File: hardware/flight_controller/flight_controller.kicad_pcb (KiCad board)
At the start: 2 copper layers, 2 parts, among them U1 Teensy3.6

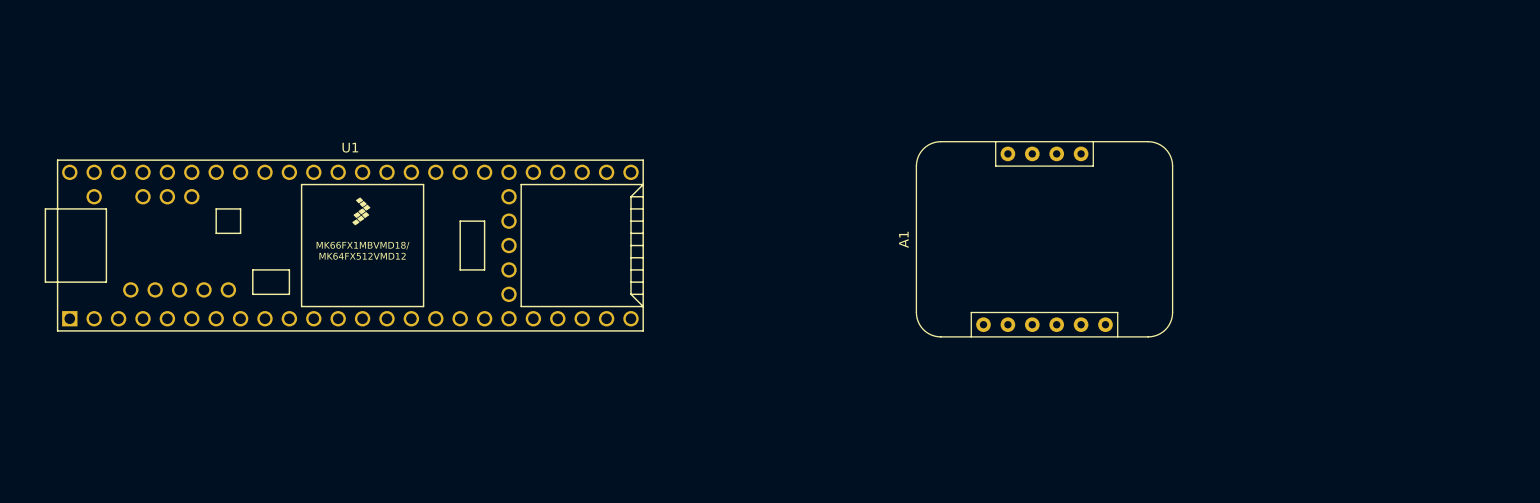
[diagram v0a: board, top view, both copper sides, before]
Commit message: PCB design for flight controller is basically complete. Need to verify and have fun with the design before ordering
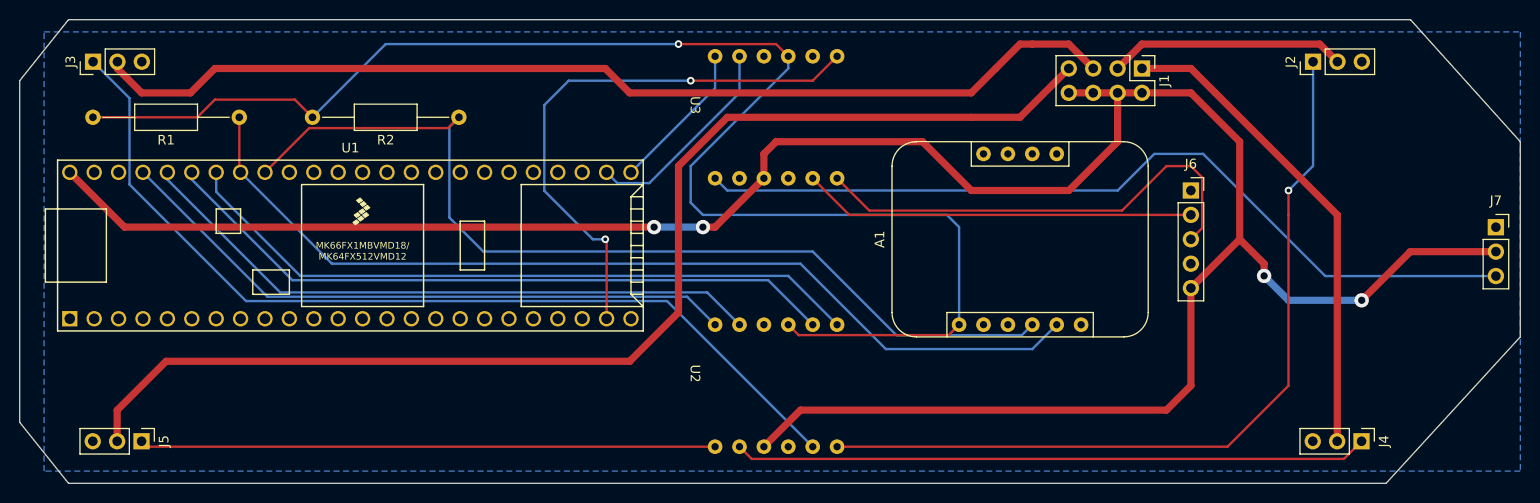
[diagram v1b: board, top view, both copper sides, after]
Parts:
- added J1: Conn_02x04_Odd_Even, Connector_PinHeader_2.54mm:PinHeader_2x04_P2.54mm_Vertical, F.Cu at (213.3, 88.9)
- added J2: Conn_01x03, Connector_PinHeader_2.54mm:PinHeader_1x03_P2.54mm_Vertical, F.Cu at (231.2, 88.2)
- added J3: Conn_01x03, Connector_PinHeader_2.54mm:PinHeader_1x03_P2.54mm_Vertical, F.Cu at (104.2, 88.2)
- added J4: Conn_01x03, Connector_PinHeader_2.54mm:PinHeader_1x03_P2.54mm_Vertical, F.Cu at (236.2, 127.7)
- added J5: Conn_01x03, Connector_PinHeader_2.54mm:PinHeader_1x03_P2.54mm_Vertical, F.Cu at (109.2, 127.7)
- added J6: Conn_01x05, Connector_PinSocket_2.54mm:PinSocket_1x05_P2.54mm_Vertical, F.Cu at (218.4, 101.6)
- added J7: Conn_01x03, Connector_PinSocket_2.54mm:PinSocket_1x03_P2.54mm_Vertical, F.Cu at (250.2, 105.4)
- added R1: 1k, Resistor_THT:R_Axial_DIN0207_L6.3mm_D2.5mm_P15.24mm_Horizontal, F.Cu at (119.4, 94.0)
- added R2: 1k, Resistor_THT:R_Axial_DIN0207_L6.3mm_D2.5mm_P15.24mm_Horizontal, F.Cu at (142.2, 94.0)
- added U2: Logic_Level_Converter, KleiCad:Logic_Level_Converter, F.Cu at (171.4, 120.7)
- added U3: Logic_Level_Converter, KleiCad:Logic_Level_Converter, F.Cu at (171.4, 92.7)
- U1: footprint Teensy:Teensy35_36 -> Teensy:Teensy35_36_outerpins
- moved A1 2.54 mm to (200.7, 106.7)
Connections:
- A1 pad 1: Net-(A1-Pad1) -> 3.3V
- A1 pad 3: unconnected-(A1-Pad3) -> GND
- U1 pad 1: unconnected-(U1-Pad1) -> GND
- U1 pad 23: unconnected-(U1-Pad23) -> RX4
- U1 pad 24: unconnected-(U1-Pad24) -> TX4
- U1 pad 30: unconnected-(U1-Pad30) -> TX5
- U1 pad 31: unconnected-(U1-Pad31) -> RX5
- U1 pad 39: unconnected-(U1-Pad39) -> GND
- U1 pad 47: unconnected-(U1-Pad47) -> A6
- U1 pad 48: unconnected-(U1-Pad48) -> A7
- U1 pad 49: unconnected-(U1-Pad49) -> A8
- U1 pad 50: unconnected-(U1-Pad50) -> A9
- U1 pad 53: unconnected-(U1-Pad53) -> 5V_VIN
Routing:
- net 5V_VIN: track 0.00 -> 252.5 mm, vias 0 -> 4
- net 3.3V: track 0.00 -> 154.9 mm, vias 0 -> 1
- net VIN_BR: track 0.00 -> 126.0 mm
- net VIN_BL: track 0.00 -> 108.6 mm
- net Net-(A1-Pad4): track 0.00 -> 99.6 mm
- net Net-(A1-Pad5): track 0.00 -> 99.4 mm
- net MOTOR_BL: track 0.00 -> 96.8 mm
- net iA6b_motors: track 0.00 -> 88.7 mm
- net MOTOR_FL: track 0.00 -> 84.4 mm, vias 0 -> 1
- net A6: track 0.00 -> 72.4 mm
- net A7: track 0.00 -> 71.6 mm
- net A8: track 0.00 -> 66.6 mm
- net A9: track 0.00 -> 66.1 mm
- net MOTOR_FR: track 0.00 -> 66.0 mm
- net MOTOR_BR: track 0.00 -> 59.9 mm
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- added copper zone on B.Cu, net GND
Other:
- board outline added: 156.2 x 48.3 mm
